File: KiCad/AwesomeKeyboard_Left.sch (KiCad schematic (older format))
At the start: 56 parts, among them J1 AudioJack4_Ground, SW1 SW_DIP_x01, SW11 SW_Push, SW12 SW_Push, SW13 SW_Push, SW14 SW_Push, SW15 SW_Push, SW16 SW_Push, SW21 SW_Push, SW22 SW_Push, SW23 SW_Push, SW24 SW_Push, SW25 SW_Push, SW26 SW_Push, SW31 SW_Push, SW32 SW_Push, SW33 SW_Push, SW34 SW_Push, SW35 SW_Push, SW36 SW_Push, SW45 SW_Push, SW46 SW_Push

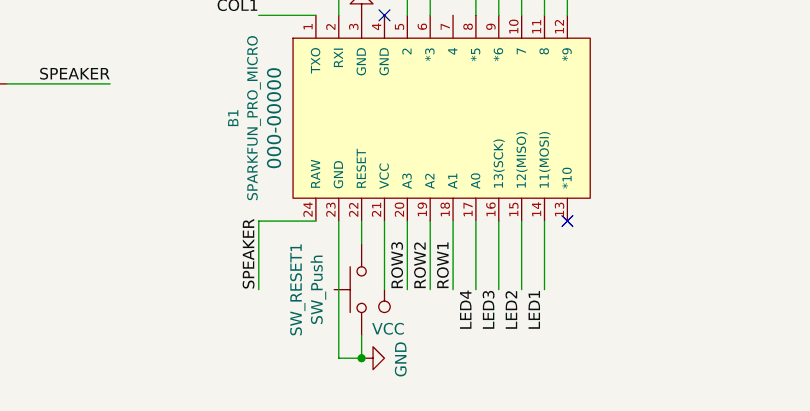
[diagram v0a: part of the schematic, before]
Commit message: add bypass condenser
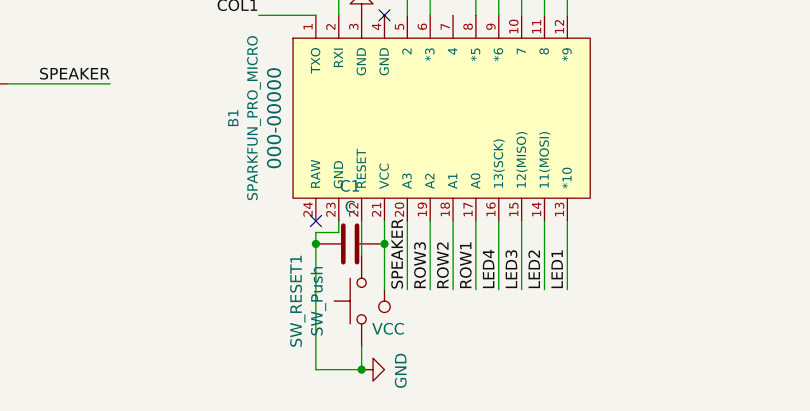
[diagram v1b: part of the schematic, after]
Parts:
- added C1: C, Capacitor_SMD:CP_Elec_3x5.3, symbol Device:C
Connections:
- net GND: now also C1.2
- net LED1: now also B1.13 (*10); no longer B1.14 (11(MOSI))
- net LED2: now also B1.14 (11(MOSI)); no longer B1.15 (12(MISO))
- net LED3: now also B1.15 (12(MISO)); no longer B1.16 (13(SCK))
- net LED4: now also B1.16 (13(SCK)); no longer B1.17 (A0)
- net ROW1: now also B1.17 (A0); no longer B1.18 (A1)
- net ROW2: now also B1.18 (A1); no longer B1.19 (A2)
- net ROW3: now also B1.19 (A2); no longer B1.20 (A3)
- net SPEAKER: now also B1.20 (A3); no longer B1.24 (RAW)
- net VCC: now also C1.1
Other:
- moved on the sheet: SW_RESET1
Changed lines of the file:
@@
 Wire Wire Line
 	5350 5650 5350 5350
+Text Label 5050 6850 1    50   ~ 0
+ROW1
 Text Label 4950 6850 1    50   ~ 0
-ROW1
+ROW2
 Text Label 4850 6850 1    50   ~ 0
-ROW2
-Text Label 4750 6850 1    50   ~ 0
 ROW3
 Wire Wire Line
+	5050 6550 5050 6850
+Wire Wire Line
 	4950 6550 4950 6850
 Wire Wire Line
 	4850 6550 4850 6850
 Wire Wire Line
-	4750 6550 4750 6850
-Wire Wire Line
-	5250 6550 5250 6850
-Text Label 5250 6850 3    50   ~ 0
+	5350 6550 5350 6850
+Text Label 5350 6850 1    50   ~ 0
 LED2
-Text Label 5350 6850 3    50   ~ 0
+Text Label 5450 6850 1    50   ~ 0
 LED1
 Text Label 5050 5350 3    50   ~ 0
@@
 ROW4
 Wire Wire Line
-	5350 6550 5350 6850
+	5450 6550 5450 6850
 Wire Wire Line
 	5050 5350 5050 5650
@@
 	0    -1   1    0
 $EndComp
-Text Label 4100 6850 1    50   ~ 0
+Text Label 4750 6850 1    50   ~ 0
 SPEAKER
 $Comp
 L Switch:SW_Push SW_RESET1
 U 1 1 5BF8FEF5
-P 4550 6850
-F 0 "SW_RESET1" H 4550 7135 50  0000 C CNN
-F 1 "SW_Push" H 4550 7044 50  0000 C CNN
-F 2 "Button_Switch_SMD:SW_SPST_FSMSM" H 4550 7050 50  0001 C CNN
-F 3 "" H 4550 7050 50  0001 C CNN
-	1    4550 6850
-	0    -1   1    0
-$EndComp
-Wire Wire Line
-	4550 6550 4550 6650
+P 4550 6900
+F 0 "SW_RESET1" H 4550 7185 50  0000 C CNN
+F 1 "SW_Push" H 4550 7094 50  0000 C CNN
+F 2 "Button_Switch_SMD:SW_SPST_FSMSM" H 4550 7100 50  0001 C CNN
+F 3 "" H 4550 7100 50  0001 C CNN
+	1    4550 6900
+	0    -1   1    0
+$EndComp
 $Comp
 L Device:Speaker LS1
@@
 $EndComp
 Wire Wire Line
+	5250 6550 5250 6850
+Wire Wire Line
 	5150 6550 5150 6850
-Wire Wire Line
-	5050 6550 5050 6850
-Text Label 5150 6850 3    50   ~ 0
+Text Label 5250 6850 1    50   ~ 0
 LED3
-Text Label 5050 6850 3    50   ~ 0
+Text Label 5150 6850 1    50   ~ 0
 LED4
 Text Label 4100 5550 2    50   ~ 0
@@
 $EndComp
 Wire Wire Line
-	4550 7050 4550 7150
-Wire Wire Line
-	4450 7150 4550 7150
-Wire Wire Line
-	4450 6550 4450 7150
-Wire Wire Line
-	4650 6850 4650 6550
+	4550 7100 4550 7200
+Wire Wire Line
+	4350 6600 4350 6650
+Wire Wire Line
+	4650 6850 4650 6650
 $Comp
 L power:VCC #PWR0104
@@
 	1    0    0    1
 $EndComp
-Connection ~ 4550 7150
+Connection ~ 4550 7200
 $Comp
 L power:GND #PWR0103
 U 1 1 5BF8AB0F
-P 4550 7150
-F 0 "#PWR0103" H 4550 6900 50  0001 C CNN
-F 1 "GND" H 4555 6977 50  0000 C CNN
-F 2 "" H 4550 7150 50  0001 C CNN
-F 3 "" H 4550 7150 50  0001 C CNN
-	1    4550 7150
+P 4550 7200
+F 0 "#PWR0103" H 4550 6950 50  0001 C CNN
+F 1 "GND" H 4555 7027 50  0000 C CNN
+F 2 "" H 4550 7200 50  0001 C CNN
+F 3 "" H 4550 7200 50  0001 C CNN
+	1    4550 7200
 	0    -1   1    0
 $EndComp
@@
 Text Label 5350 5350 3    50   ~ 0
 COL6
-NoConn ~ 5450 6550
 NoConn ~ 4650 5650
 Wire Wire Line
-	4100 6550 4350 6550
-Wire Wire Line
-	4100 6550 4100 6850
-$Comp
-L power:GND #PWR?
+	4750 6550 4750 6850
+$Comp
+L power:GND #PWR0105
 U 1 1 5C06FE4D
 P 4550 5650
-F 0 "#PWR?" H 4550 5400 50  0001 C CNN
+F 0 "#PWR0105" H 4550 5400 50  0001 C CNN
 F 1 "GND" H 4555 5477 50  0000 C CNN
 F 2 "" H 4550 5650 50  0001 C CNN
@@
 	-1   0    0    1
 $EndComp
+NoConn ~ 4350 6550
+$Comp
+L Device:C C1
+U 1 1 5C08A9E4
+P 4500 6650
+F 0 "C1" V 4248 6650 50  0000 C CNN
+F 1 "C" V 4339 6650 50  0000 C CNN
+F 2 "Capacitor_SMD:CP_Elec_3x5.3" H 4538 6500 50  0001 C CNN
+F 3 "~" H 4500 6650 50  0001 C CNN
+	1    4500 6650
+	0    1    1    0
+$EndComp
+Connection ~ 4650 6650
+Wire Wire Line
+	4650 6650 4650 6550
+Connection ~ 4350 6650
+Wire Wire Line
+	4350 6650 4350 7200
+Wire Wire Line
+	4550 6550 4550 6700
+Wire Wire Line
+	4350 7200 4550 7200
+Wire Wire Line
+	4350 6600 4450 6600
+Wire Wire Line
+	4450 6600 4450 6550
 $EndSCHEMATC

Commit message: modify
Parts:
- C1: footprint Capacitor_SMD:CP_Elec_3x5.3 -> Capacitor_THT:CP_Axial_L10.0mm_D4.5mm_P15.00mm_Horizontal
- D11, D12, D13, D14, D15, D16, D21, D22, D23, D24, D25, D26, D31, D32, D33, D34, D35, D36, D45, D46: footprint Diode_SMD:D_SOD-123 -> Diode_THT:D_DO-35_SOD27_P7.62mm_Horizontal
- LS1: footprint Buzzer_Beeper:Buzzer_Murata_PKMCS0909E4000-R1 -> Buzzer_Beeper:Buzzer_12x9.5RM7.6
- SW1: footprint Button_Switch_SMD:SW_DIP_SPSTx01_Slide_6.7x4.1mm_W6.73mm_P2.54mm_LowProfile_JPin -> Button_Switch_THT:SW_DIP_SPSTx01_Slide_6.7x4.1mm_W7.62mm_P2.54mm_LowProfile
- SW_RESET1: footprint Button_Switch_SMD:SW_SPST_FSMSM -> Button_Switch_THT:SW_PUSH_6mm
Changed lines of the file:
@@
 F 0 "D11" H 3900 2365 50  0000 C CNN
 F 1 "DIODE" H 3900 2274 50  0000 C CNN
-F 2 "Diode_SMD:D_SOD-123" H 3900 2100 50  0001 C CNN
+F 2 "Diode_THT:D_DO-35_SOD27_P7.62mm_Horizontal" H 3900 2100 50  0001 C CNN
 F 3 "~" H 3900 2100 50  0001 C CNN
 	1    3900 2100
@@
 F 0 "D16" H 7650 2365 50  0000 C CNN
 F 1 "DIODE" H 7650 2274 50  0000 C CNN
-F 2 "Diode_SMD:D_SOD-123" H 7650 2100 50  0001 C CNN
+F 2 "Diode_THT:D_DO-35_SOD27_P7.62mm_Horizontal" H 7650 2100 50  0001 C CNN
 F 3 "~" H 7650 2100 50  0001 C CNN
 	1    7650 2100
@@
 F 0 "D15" H 6900 2365 50  0000 C CNN
 F 1 "DIODE" H 6900 2274 50  0000 C CNN
-F 2 "Diode_SMD:D_SOD-123" H 6900 2100 50  0001 C CNN
+F 2 "Diode_THT:D_DO-35_SOD27_P7.62mm_Horizontal" H 6900 2100 50  0001 C CNN
 F 3 "~" H 6900 2100 50  0001 C CNN
 	1    6900 2100
@@
 F 0 "D14" H 6150 2365 50  0000 C CNN
 F 1 "DIODE" H 6150 2274 50  0000 C CNN
-F 2 "Diode_SMD:D_SOD-123" H 6150 2100 50  0001 C CNN
+F 2 "Diode_THT:D_DO-35_SOD27_P7.62mm_Horizontal" H 6150 2100 50  0001 C CNN
 F 3 "~" H 6150 2100 50  0001 C CNN
 	1    6150 2100
@@
 F 0 "D13" H 5400 2365 50  0000 C CNN
 F 1 "DIODE" H 5400 2274 50  0000 C CNN
-F 2 "Diode_SMD:D_SOD-123" H 5400 2100 50  0001 C CNN
+F 2 "Diode_THT:D_DO-35_SOD27_P7.62mm_Horizontal" H 5400 2100 50  0001 C CNN
 F 3 "~" H 5400 2100 50  0001 C CNN
 	1    5400 2100
@@
 F 0 "D12" H 4650 2365 50  0000 C CNN
 F 1 "DIODE" H 4650 2274 50  0000 C CNN
-F 2 "Diode_SMD:D_SOD-123" H 4650 2100 50  0001 C CNN
+F 2 "Diode_THT:D_DO-35_SOD27_P7.62mm_Horizontal" H 4650 2100 50  0001 C CNN
 F 3 "~" H 4650 2100 50  0001 C CNN
 	1    4650 2100
@@
 F 0 "D36" H 7650 3765 50  0000 C CNN
 F 1 "DIODE" H 7650 3674 50  0000 C CNN
-F 2 "Diode_SMD:D_SOD-123" H 7650 3500 50  0001 C CNN
+F 2 "Diode_THT:D_DO-35_SOD27_P7.62mm_Horizontal" H 7650 3500 50  0001 C CNN
 F 3 "~" H 7650 3500 50  0001 C CNN
 	1    7650 3500
@@
 F 0 "D35" H 6900 3765 50  0000 C CNN
 F 1 "DIODE" H 6900 3674 50  0000 C CNN
-F 2 "Diode_SMD:D_SOD-123" H 6900 3500 50  0001 C CNN
+F 2 "Diode_THT:D_DO-35_SOD27_P7.62mm_Horizontal" H 6900 3500 50  0001 C CNN
 F 3 "~" H 6900 3500 50  0001 C CNN
 	1    6900 3500
@@
 F 0 "D26" H 7650 3065 50  0000 C CNN
 F 1 "DIODE" H 7650 2974 50  0000 C CNN
-F 2 "Diode_SMD:D_SOD-123" H 7650 2800 50  0001 C CNN
+F 2 "Diode_THT:D_DO-35_SOD27_P7.62mm_Horizontal" H 7650 2800 50  0001 C CNN
 F 3 "~" H 7650 2800 50  0001 C CNN
 	1    7650 2800
@@
 F 0 "D25" H 6900 3065 50  0000 C CNN
 F 1 "DIODE" H 6900 2974 50  0000 C CNN
-F 2 "Diode_SMD:D_SOD-123" H 6900 2800 50  0001 C CNN
+F 2 "Diode_THT:D_DO-35_SOD27_P7.62mm_Horizontal" H 6900 2800 50  0001 C CNN
 F 3 "~" H 6900 2800 50  0001 C CNN
 	1    6900 2800
@@
 F 0 "D34" H 6150 3765 50  0000 C CNN
 F 1 "DIODE" H 6150 3674 50  0000 C CNN
-F 2 "Diode_SMD:D_SOD-123" H 6150 3500 50  0001 C CNN
+F 2 "Diode_THT:D_DO-35_SOD27_P7.62mm_Horizontal" H 6150 3500 50  0001 C CNN
 F 3 "~" H 6150 3500 50  0001 C CNN
 	1    6150 3500
@@
 F 0 "D33" H 5400 3765 50  0000 C CNN
 F 1 "DIODE" H 5400 3674 50  0000 C CNN
-F 2 "Diode_SMD:D_SOD-123" H 5400 3500 50  0001 C CNN
+F 2 "Diode_THT:D_DO-35_SOD27_P7.62mm_Horizontal" H 5400 3500 50  0001 C CNN
 F 3 "~" H 5400 3500 50  0001 C CNN
 	1    5400 3500
@@
 F 0 "D24" H 6150 3065 50  0000 C CNN
 F 1 "DIODE" H 6150 2974 50  0000 C CNN
-F 2 "Diode_SMD:D_SOD-123" H 6150 2800 50  0001 C CNN
+F 2 "Diode_THT:D_DO-35_SOD27_P7.62mm_Horizontal" H 6150 2800 50  0001 C CNN
 F 3 "~" H 6150 2800 50  0001 C CNN
 	1    6150 2800
@@
 F 0 "D23" H 5400 3065 50  0000 C CNN
 F 1 "DIODE" H 5400 2974 50  0000 C CNN
-F 2 "Diode_SMD:D_SOD-123" H 5400 2800 50  0001 C CNN
+F 2 "Diode_THT:D_DO-35_SOD27_P7.62mm_Horizontal" H 5400 2800 50  0001 C CNN
 F 3 "~" H 5400 2800 50  0001 C CNN
 	1    5400 2800
@@
 F 0 "D46" H 7650 4465 50  0000 C CNN
 F 1 "DIODE" H 7650 4374 50  0000 C CNN
-F 2 "Diode_SMD:D_SOD-123" H 7650 4200 50  0001 C CNN
+F 2 "Diode_THT:D_DO-35_SOD27_P7.62mm_Horizontal" H 7650 4200 50  0001 C CNN
 F 3 "~" H 7650 4200 50  0001 C CNN
 	1    7650 4200
@@
 F 0 "D45" H 6900 4465 50  0000 C CNN
 F 1 "DIODE" H 6900 4374 50  0000 C CNN
-F 2 "Diode_SMD:D_SOD-123" H 6900 4200 50  0001 C CNN
+F 2 "Diode_THT:D_DO-35_SOD27_P7.62mm_Horizontal" H 6900 4200 50  0001 C CNN
 F 3 "~" H 6900 4200 50  0001 C CNN
 	1    6900 4200
@@
 F 0 "D32" H 4650 3765 50  0000 C CNN
 F 1 "DIODE" H 4650 3674 50  0000 C CNN
-F 2 "Diode_SMD:D_SOD-123" H 4650 3500 50  0001 C CNN
+F 2 "Diode_THT:D_DO-35_SOD27_P7.62mm_Horizontal" H 4650 3500 50  0001 C CNN
 F 3 "~" H 4650 3500 50  0001 C CNN
 	1    4650 3500
@@
 F 0 "D31" H 3900 3765 50  0000 C CNN
 F 1 "DIODE" H 3900 3674 50  0000 C CNN
-F 2 "Diode_SMD:D_SOD-123" H 3900 3500 50  0001 C CNN
+F 2 "Diode_THT:D_DO-35_SOD27_P7.62mm_Horizontal" H 3900 3500 50  0001 C CNN
 F 3 "~" H 3900 3500 50  0001 C CNN
 	1    3900 3500
@@
 F 0 "D22" H 4650 3065 50  0000 C CNN
 F 1 "DIODE" H 4650 2974 50  0000 C CNN
-F 2 "Diode_SMD:D_SOD-123" H 4650 2800 50  0001 C CNN
+F 2 "Diode_THT:D_DO-35_SOD27_P7.62mm_Horizontal" H 4650 2800 50  0001 C CNN
 F 3 "~" H 4650 2800 50  0001 C CNN
 	1    4650 2800
@@
 F 0 "D21" H 3900 3065 50  0000 C CNN
 F 1 "DIODE" H 3900 2974 50  0000 C CNN
-F 2 "Diode_SMD:D_SOD-123" H 3900 2800 50  0001 C CNN
+F 2 "Diode_THT:D_DO-35_SOD27_P7.62mm_Horizontal" H 3900 2800 50  0001 C CNN
 F 3 "~" H 3900 2800 50  0001 C CNN
 	1    3900 2800
@@
 F 0 "SW_RESET1" H 4550 7185 50  0000 C CNN
 F 1 "SW_Push" H 4550 7094 50  0000 C CNN
-F 2 "Button_Switch_SMD:SW_SPST_FSMSM" H 4550 7100 50  0001 C CNN
+F 2 "Button_Switch_THT:SW_PUSH_6mm" H 4550 7100 50  0001 C CNN
 F 3 "" H 4550 7100 50  0001 C CNN
 	1    4550 6900
@@
 F 0 "LS1" H 2070 5946 50  0000 L CNN
 F 1 "Speaker" H 2070 5855 50  0000 L CNN
-F 2 "Buzzer_Beeper:Buzzer_Murata_PKMCS0909E4000-R1" H 1900 5750 50  0001 C CNN
+F 2 "Buzzer_Beeper:Buzzer_12x9.5RM7.6" H 1900 5750 50  0001 C CNN
 F 3 "~" H 1890 5900 50  0001 C CNN
 	1    1900 5950
@@
 F 0 "SW1" H 2700 6217 50  0000 C CNN
 F 1 "SW_DIP_x01" H 2700 6126 50  0000 C CNN
-F 2 "Button_Switch_SMD:SW_DIP_SPSTx01_Slide_6.7x4.1mm_W6.73mm_P2.54mm_LowProfile_JPin" H 2700 5950 50  0001 C CNN
+F 2 "Button_Switch_THT:SW_DIP_SPSTx01_Slide_6.7x4.1mm_W7.62mm_P2.54mm_LowProfile" H 2700 5950 50  0001 C CNN
 F 3 "" H 2700 5950 50  0001 C CNN
 	1    2700 5950
@@
 F 0 "C1" V 4248 6650 50  0000 C CNN
 F 1 "C" V 4339 6650 50  0000 C CNN
-F 2 "Capacitor_SMD:CP_Elec_3x5.3" H 4538 6500 50  0001 C CNN
+F 2 "Capacitor_THT:CP_Axial_L10.0mm_D4.5mm_P15.00mm_Horizontal" H 4538 6500 50  0001 C CNN
 F 3 "~" H 4500 6650 50  0001 C CNN
 	1    4500 6650
